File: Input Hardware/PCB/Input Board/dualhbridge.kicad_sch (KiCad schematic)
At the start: 10 parts, among them U1101 74HCS95, U1102 DRV8837, U1103 DRV8837, U1104 DRV8837, U1105 DRV8837

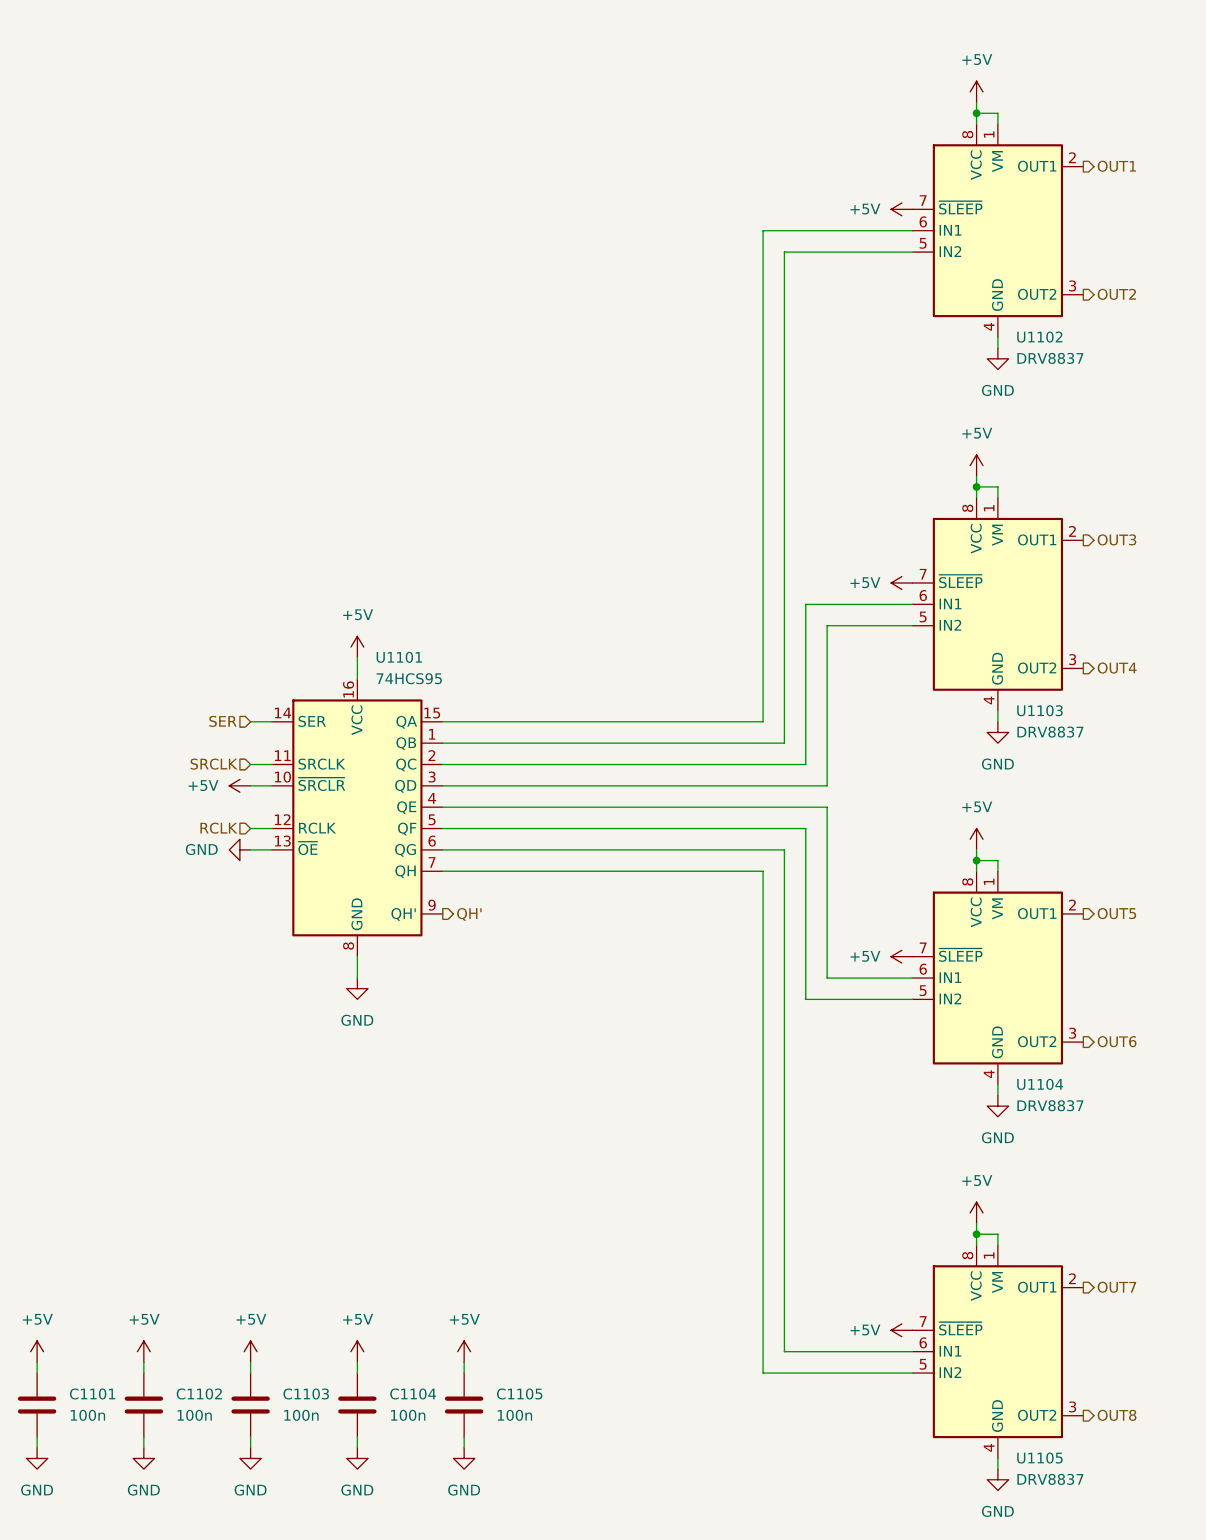
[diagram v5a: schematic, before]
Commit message: sleep pin rewire
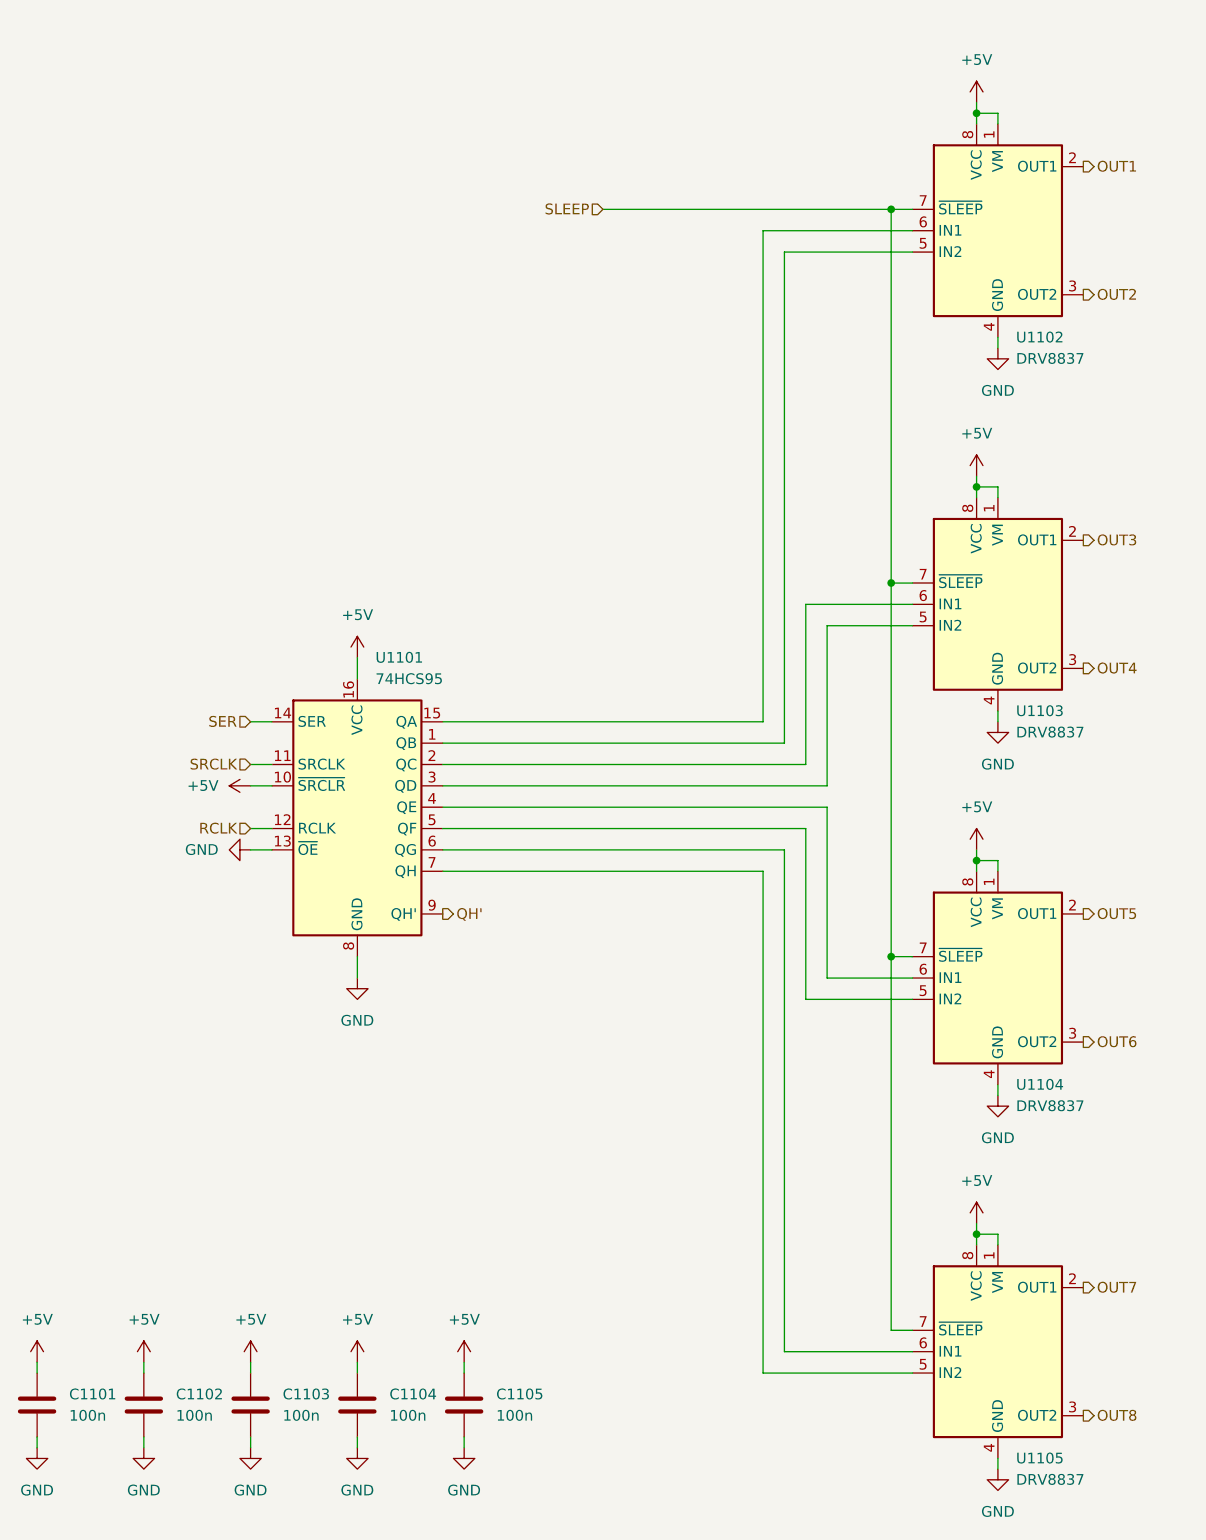
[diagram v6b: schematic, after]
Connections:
- net +5V: no longer U1102.7 (~{SLEEP}), U1103.7 (~{SLEEP}), U1104.7 (~{SLEEP}), U1105.7 (~{SLEEP})
- new net SLEEP: U1102.7 (~{SLEEP}), U1103.7 (~{SLEEP}), U1104.7 (~{SLEEP}), U1105.7 (~{SLEEP})
